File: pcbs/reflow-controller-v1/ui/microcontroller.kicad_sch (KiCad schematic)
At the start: 15 parts, among them J3 SWD, J4 UART, U3 STM32G474VETx

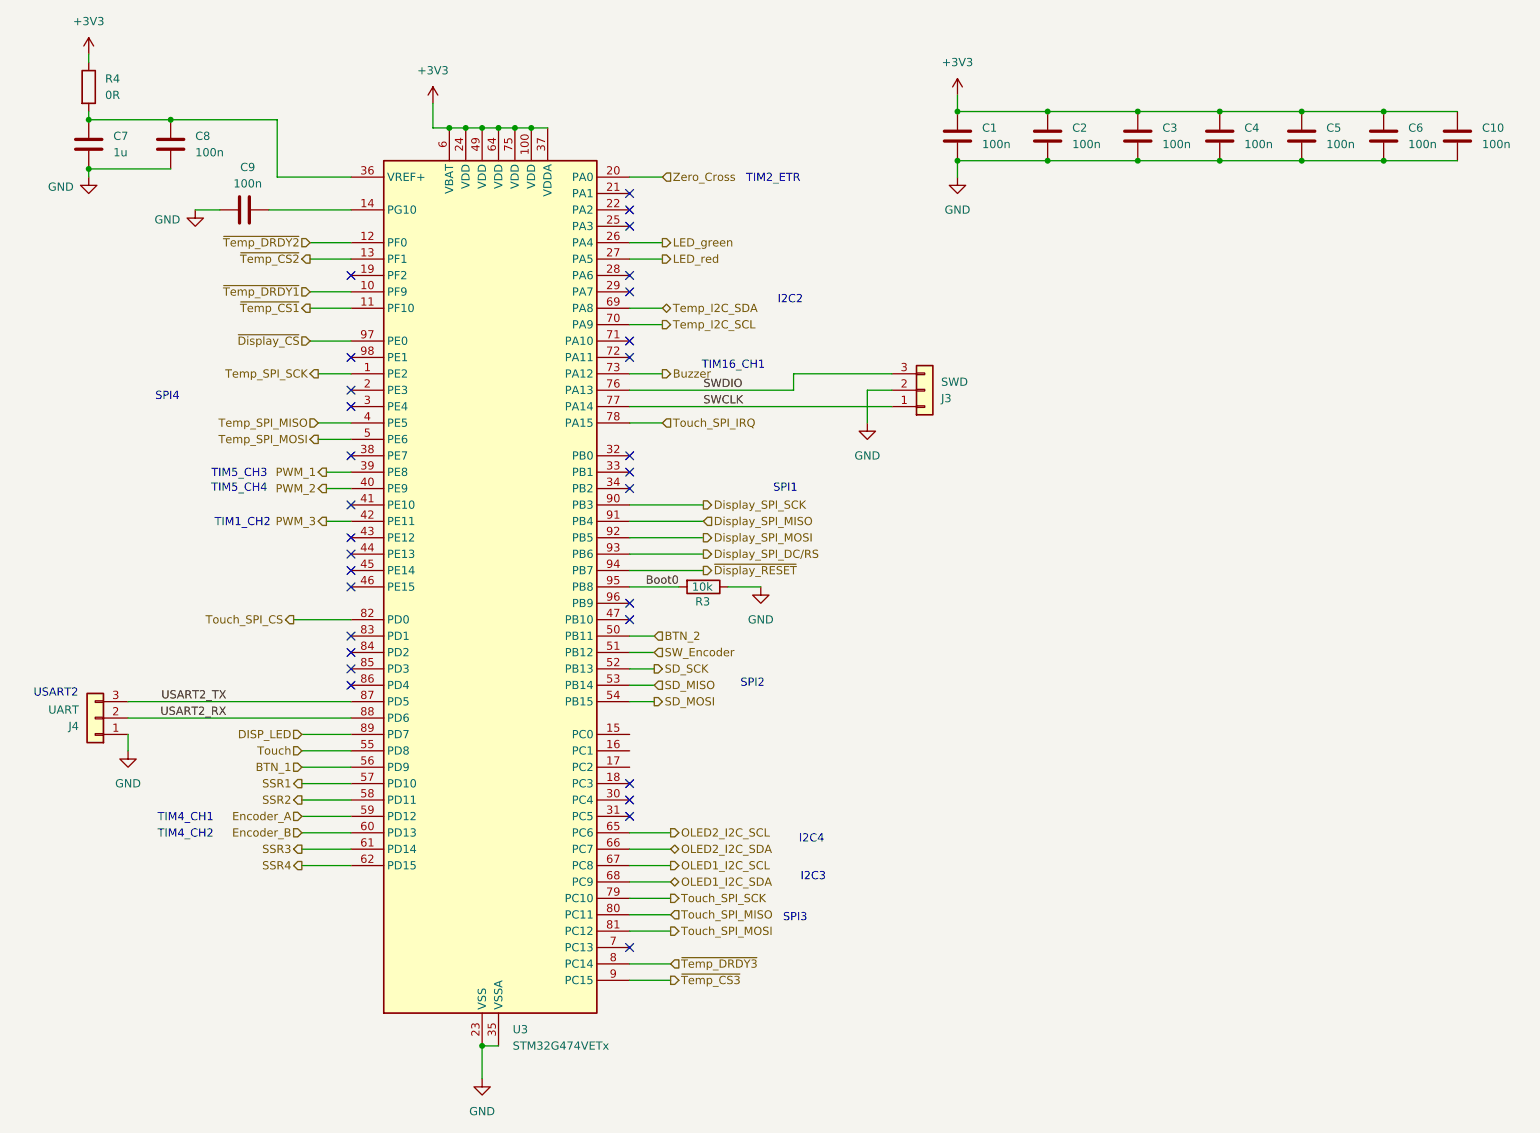
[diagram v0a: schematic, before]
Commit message: split pcbs into two for safety
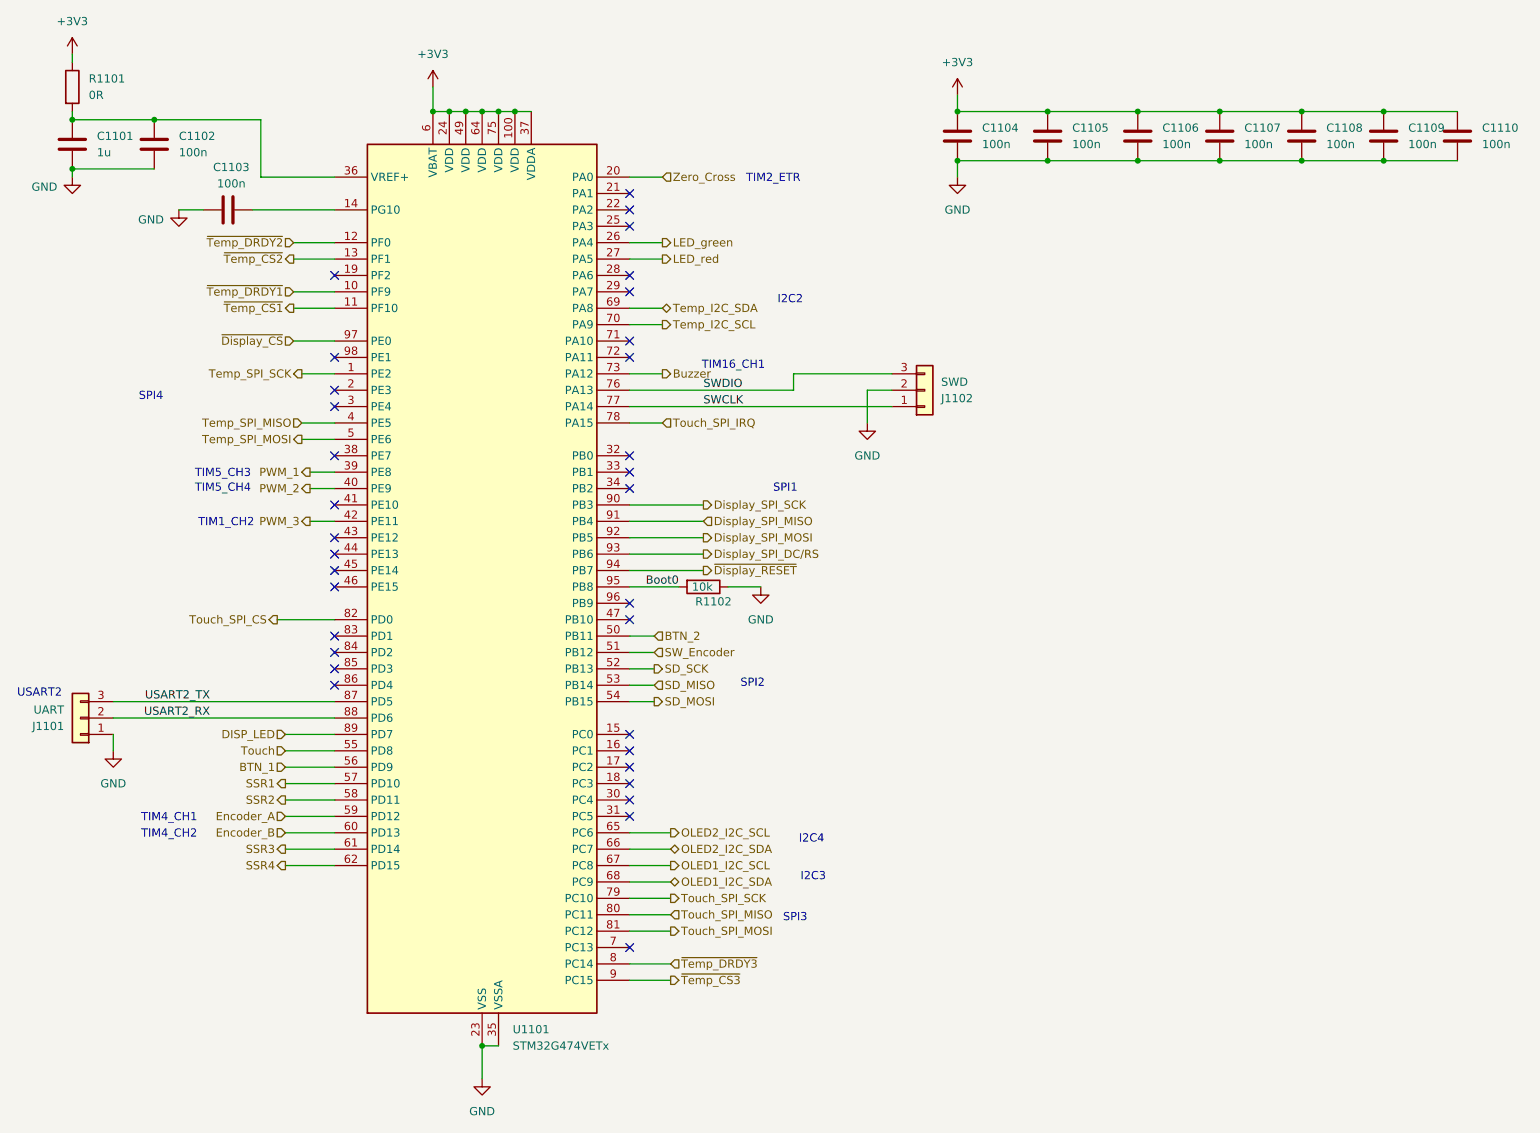
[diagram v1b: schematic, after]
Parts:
- renumbered C7 to C1101, C8 to C1102, C9 to C1103, C1 to C1104, C2 to C1105, C3 to C1106, C4 to C1107, C5 to C1108, C6 to C1109, C10 to C1110, J4 to J1101, J3 to J1102, R4 to R1101, R3 to R1102, U3 to U1101
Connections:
- no-connect marks 30 -> 33
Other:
- moved on the sheet: C1101, C1102, C1103, J1101, R1101, U1101
